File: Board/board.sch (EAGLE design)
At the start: 51 parts, among them IC1 L297, IC2 MEGA32-P, IC3 L298, J1 +12V, Q1 BC639, Q3 BC639, U2 DS1621+, X1 WATER_PUMP, X2 FAN, X5 SM_CD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

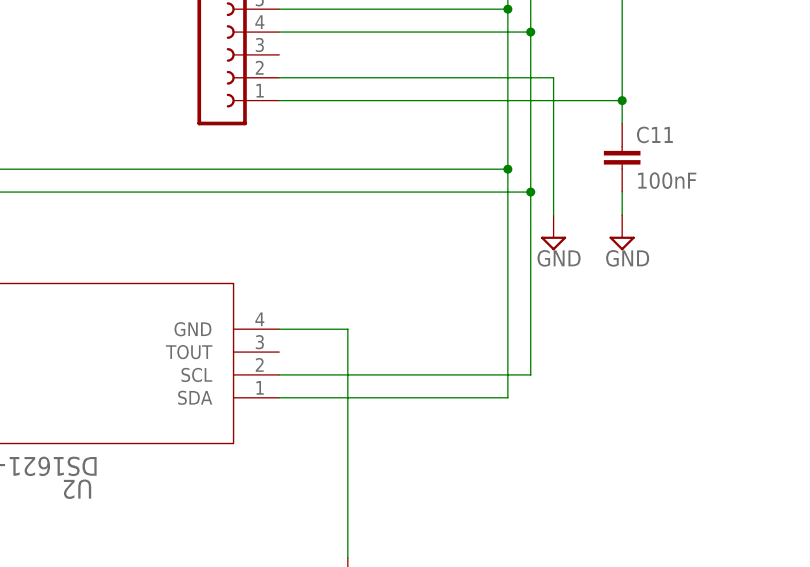
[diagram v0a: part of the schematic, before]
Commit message: SCL/SDA thermometer
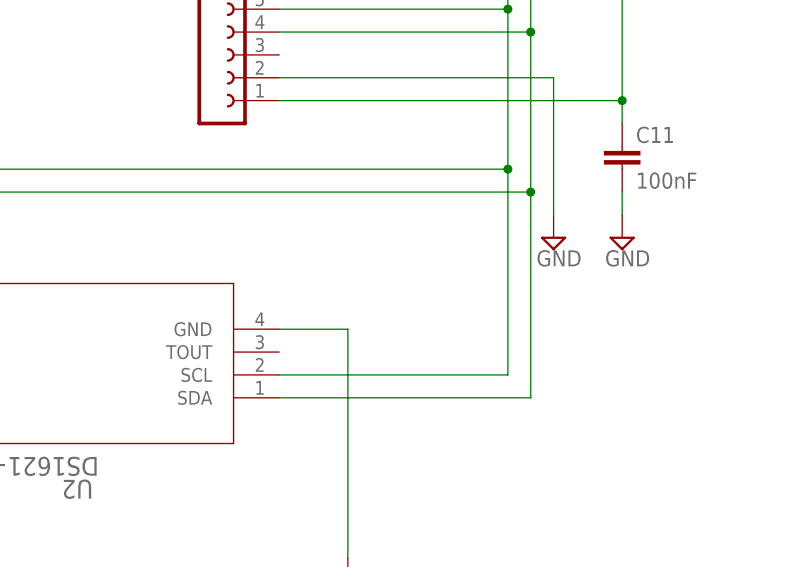
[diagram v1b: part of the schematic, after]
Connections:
- net N$35: now also U2.SDA; no longer U2.SCL
- net N$36: now also U2.SCL; no longer U2.SDA
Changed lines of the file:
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@@
 <grid distance="0.1" unitdist="inch" unit="inch" style="lines" multiple="1" display="no" altdistance="0.01" altunitdist="inch" altunit="inch"/>
 <layers>
-<layer number="1" name="Top" color="4" fill="1" visible="no" active="no"/>
-<layer number="2" name="Route2" color="1" fill="3" visible="no" active="no"/>
-<layer number="3" name="Route3" color="4" fill="3" visible="no" active="no"/>
-<layer number="4" name="Route4" color="1" fill="4" visible="no" active="no"/>
-<layer number="5" name="Route5" color="4" fill="4" visible="no" active="no"/>
-<layer number="6" name="Route6" color="1" fill="8" visible="no" active="no"/>
-<layer number="7" name="Route7" color="4" fill="8" visible="no" active="no"/>
-<layer number="8" name="Route8" color="1" fill="2" visible="no" active="no"/>
-<layer number="9" name="Route9" color="4" fill="2" visible="no" active="no"/>
-<layer number="10" name="Route10" color="1" fill="7" visible="no" active="no"/>
-<layer number="11" name="Route11" color="4" fill="7" visible="no" active="no"/>
-<layer number="12" name="Route12" color="1" fill="5" visible="no" active="no"/>
-<layer number="13" name="Route13" color="4" fill="5" visible="no" active="no"/>
-<layer number="14" name="Route14" color="1" fill="6" visible="no" active="no"/>
-<layer number="15" name="Route15" color="4" fill="6" visible="no" active="no"/>
-<layer number="16" name="Bottom" color="1" fill="1" visible="no" active="no"/>
-<layer number="17" name="Pads" color="2" fill="1" visible="no" active="no"/>
-<layer number="18" name="Vias" color="2" fill="1" visible="no" active="no"/>
-<layer number="19" name="Unrouted" color="6" fill="1" visible="no" active="no"/>
-<layer number="20" name="Dimension" color="24" fill="1" visible="no" active="no"/>
-<layer number="21" name="tPlace" color="7" fill="1" visible="no" active="no"/>
-<layer number="22" name="bPlace" color="7" fill="1" visible="no" active="no"/>
-<layer number="23" name="tOrigins" color="15" fill="1" visible="no" active="no"/>
-<layer number="24" name="bOrigins" color="15" fill="1" visible="no" active="no"/>
-<layer number="25" name="tNames" color="7" fill="1" visible="no" active="no"/>
-<layer number="26" name="bNames" color="7" fill="1" visible="no" active="no"/>
-<layer number="27" name="tValues" color="7" fill="1" visible="no" active="no"/>
-<layer number="28" name="bValues" color="7" fill="1" visible="no" active="no"/>
+<layer number="1" name="Top" color="4" fill="1" visible="yes" active="no"/>
+<layer number="2" name="Route2" color="1" fill="3" visible="yes" active="no"/>
+<layer number="3" name="Route3" color="4" fill="3" visible="yes" active="no"/>
+<layer number="4" name="Route4" color="1" fill="4" visible="yes" active="no"/>
+<layer number="5" name="Route5" color="4" fill="4" visible="yes" active="no"/>
+<layer number="6" name="Route6" color="1" fill="8" visible="yes" active="no"/>
+<layer number="7" name="Route7" color="4" fill="8" visible="yes" active="no"/>
+<layer number="8" name="Route8" color="1" fill="2" visible="yes" active="no"/>
+<layer number="9" name="Route9" color="4" fill="2" visible="yes" active="no"/>
+<layer number="10" name="Route10" color="1" fill="7" visible="yes" active="no"/>
+<layer number="11" name="Route11" color="4" fill="7" visible="yes" active="no"/>
+<layer number="12" name="Route12" color="1" fill="5" visible="yes" active="no"/>
+<layer number="13" name="Route13" color="4" fill="5" visible="yes" active="no"/>
+<layer number="14" name="Route14" color="1" fill="6" visible="yes" active="no"/>
+<layer number="15" name="Route15" color="4" fill="6" visible="yes" active="no"/>
+<layer number="16" name="Bottom" color="1" fill="1" visible="yes" active="no"/>
+<layer number="17" name="Pads" color="2" fill="1" visible="yes" active="no"/>
+<layer number="18" name="Vias" color="2" fill="1" visible="yes" active="no"/>
+<layer number="19" name="Unrouted" color="6" fill="1" visible="yes" active="no"/>
+<layer number="20" name="Dimension" color="24" fill="1" visible="yes" active="no"/>
+<layer number="21" name="tPlace" color="7" fill="1" visible="yes" active="no"/>
+<layer number="22" name="bPlace" color="7" fill="1" visible="yes" active="no"/>
+<layer number="23" name="tOrigins" color="15" fill="1" visible="yes" active="no"/>
+<layer number="24" name="bOrigins" color="15" fill="1" visible="yes" active="no"/>
+<layer number="25" name="tNames" color="7" fill="1" visible="yes" active="no"/>
+<layer number="26" name="bNames" color="7" fill="1" visible="yes" active="no"/>
+<layer number="27" name="tValues" color="7" fill="1" visible="yes" active="no"/>
+<layer number="28" name="bValues" color="7" fill="1" visible="yes" active="no"/>
 <layer number="29" name="tStop" color="7" fill="3" visible="no" active="no"/>
 <layer number="30" name="bStop" color="7" fill="6" visible="no" active="no"/>
@@
 <layer number="35" name="tGlue" color="7" fill="4" visible="no" active="no"/>
 <layer number="36" name="bGlue" color="7" fill="5" visible="no" active="no"/>
-<layer number="37" name="tTest" color="7" fill="1" visible="no" active="no"/>
-<layer number="38" name="bTest" color="7" fill="1" visible="no" active="no"/>
+<layer number="37" name="tTest" color="7" fill="1" visible="yes" active="no"/>
+<layer number="38" name="bTest" color="7" fill="1" visible="yes" active="no"/>
 <layer number="39" name="tKeepout" color="4" fill="11" visible="no" active="no"/>
 <layer number="40" name="bKeepout" color="1" fill="11" visible="no" active="no"/>
@@
 <layer number="44" name="Drills" color="7" fill="1" visible="no" active="no"/>
 <layer number="45" name="Holes" color="7" fill="1" visible="no" active="no"/>
-<layer number="46" name="Milling" color="3" fill="1" visible="no" active="no"/>
-<layer number="47" name="Measures" color="7" fill="1" visible="no" active="no"/>
-<layer number="48" name="Document" color="7" fill="1" visible="no" active="no"/>
-<layer number="49" name="Reference" color="7" fill="1" visible="no" active="no"/>
-<layer number="50" name="dxf" color="7" fill="1" visible="no" active="no"/>
-<layer number="51" name="tDocu" color="7" fill="1" visible="no" active="no"/>
-<layer number="52" name="bDocu" color="7" fill="1" visible="no" active="no"/>
+<layer number="46" name="Milling" color="3" fill="1" visible="yes" active="no"/>
+<layer number="47" name="Measures" color="7" fill="1" visible="yes" active="no"/>
+<layer number="48" name="Document" color="7" fill="1" visible="yes" active="no"/>
+<layer number="49" name="Reference" color="7" fill="1" visible="yes" active="no"/>
+<layer number="50" name="dxf" color="7" fill="1" visible="yes" active="no"/>
+<layer number="51" name="tDocu" color="7" fill="1" visible="yes" active="no"/>
+<layer number="52" name="bDocu" color="7" fill="1" visible="yes" active="no"/>
 <layer number="88" name="SimResults" color="9" fill="1" visible="yes" active="yes"/>
 <layer number="89" name="SimProbes" color="9" fill="1" visible="yes" active="yes"/>
@@
 <wire x1="-83.82" y1="-86.36" x2="-83.82" y2="-104.14" width="0.1524" layer="91"/>
 <junction x="-83.82" y="-86.36"/>
-<pinref part="U2" gate="A" pin="SCL"/>
-<wire x1="-83.82" y1="-104.14" x2="-83.82" y2="-124.46" width="0.1524" layer="91"/>
-<wire x1="-83.82" y1="-124.46" x2="-111.76" y2="-124.46" width="0.1524" layer="91"/>
+<wire x1="-83.82" y1="-104.14" x2="-83.82" y2="-127" width="0.1524" layer="91"/>
 <pinref part="R8" gate="G$1" pin="1"/>
 <wire x1="-83.82" y1="-104.14" x2="-149.86" y2="-104.14" width="0.1524" layer="91"/>
 <wire x1="-149.86" y1="-104.14" x2="-149.86" y2="-83.82" width="0.1524" layer="91"/>
 <junction x="-83.82" y="-104.14"/>
+<pinref part="U2" gate="A" pin="SDA"/>
+<wire x1="-83.82" y1="-127" x2="-111.76" y2="-127" width="0.1524" layer="91"/>
 </segment>
 </net>
@@
 <wire x1="-86.36" y1="-83.82" x2="-86.36" y2="-101.6" width="0.1524" layer="91"/>
 <junction x="-86.36" y="-83.82"/>
-<pinref part="U2" gate="A" pin="SDA"/>
-<wire x1="-86.36" y1="-101.6" x2="-86.36" y2="-127" width="0.1524" layer="91"/>
-<wire x1="-86.36" y1="-127" x2="-111.76" y2="-127" width="0.1524" layer="91"/>
 <pinref part="R6" gate="G$1" pin="1"/>
 <wire x1="-86.36" y1="-101.6" x2="-160.02" y2="-101.6" width="0.1524" layer="91"/>
 <wire x1="-160.02" y1="-101.6" x2="-160.02" y2="-83.82" width="0.1524" layer="91"/>
+<pinref part="U2" gate="A" pin="SCL"/>
+<wire x1="-111.76" y1="-124.46" x2="-86.36" y2="-124.46" width="0.1524" layer="91"/>
+<wire x1="-86.36" y1="-124.46" x2="-86.36" y2="-101.6" width="0.1524" layer="91"/>
 <junction x="-86.36" y="-101.6"/>
 </segment>

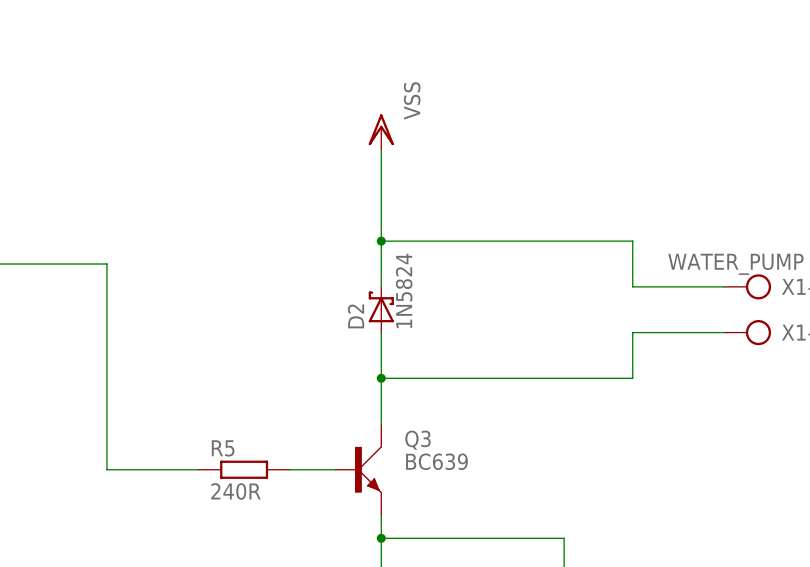
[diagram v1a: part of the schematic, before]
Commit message: Rename 1N5824 - 1N5822
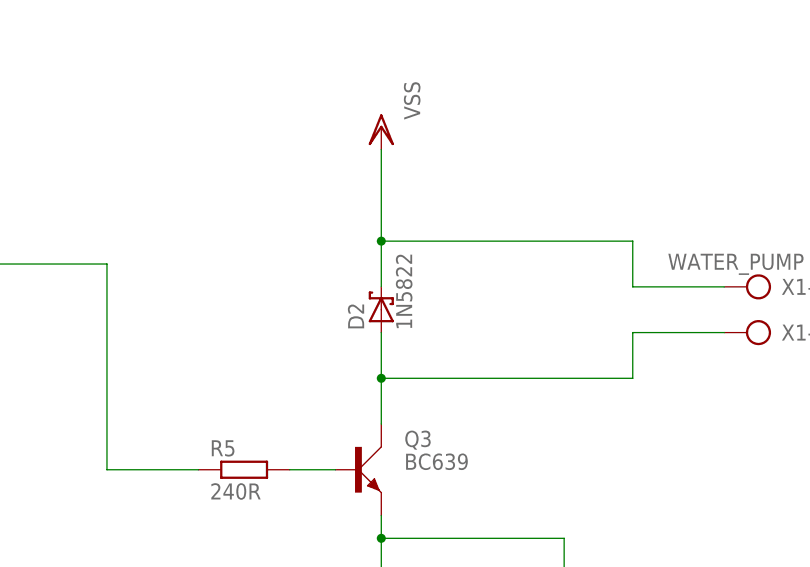
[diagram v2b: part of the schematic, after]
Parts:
- D2: value 1N5824 -> 1N5822
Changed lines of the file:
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@@
 <grid distance="0.1" unitdist="inch" unit="inch" style="lines" multiple="1" display="no" altdistance="0.01" altunitdist="inch" altunit="inch"/>
 <layers>
-<layer number="1" name="Top" color="4" fill="1" visible="yes" active="no"/>
-<layer number="2" name="Route2" color="1" fill="3" visible="yes" active="no"/>
-<layer number="3" name="Route3" color="4" fill="3" visible="yes" active="no"/>
-<layer number="4" name="Route4" color="1" fill="4" visible="yes" active="no"/>
-<layer number="5" name="Route5" color="4" fill="4" visible="yes" active="no"/>
-<layer number="6" name="Route6" color="1" fill="8" visible="yes" active="no"/>
-<layer number="7" name="Route7" color="4" fill="8" visible="yes" active="no"/>
-<layer number="8" name="Route8" color="1" fill="2" visible="yes" active="no"/>
-<layer number="9" name="Route9" color="4" fill="2" visible="yes" active="no"/>
-<layer number="10" name="Route10" color="1" fill="7" visible="yes" active="no"/>
-<layer number="11" name="Route11" color="4" fill="7" visible="yes" active="no"/>
-<layer number="12" name="Route12" color="1" fill="5" visible="yes" active="no"/>
-<layer number="13" name="Route13" color="4" fill="5" visible="yes" active="no"/>
-<layer number="14" name="Route14" color="1" fill="6" visible="yes" active="no"/>
-<layer number="15" name="Route15" color="4" fill="6" visible="yes" active="no"/>
-<layer number="16" name="Bottom" color="1" fill="1" visible="yes" active="no"/>
-<layer number="17" name="Pads" color="2" fill="1" visible="yes" active="no"/>
-<layer number="18" name="Vias" color="2" fill="1" visible="yes" active="no"/>
-<layer number="19" name="Unrouted" color="6" fill="1" visible="yes" active="no"/>
-<layer number="20" name="Dimension" color="24" fill="1" visible="yes" active="no"/>
-<layer number="21" name="tPlace" color="7" fill="1" visible="yes" active="no"/>
-<layer number="22" name="bPlace" color="7" fill="1" visible="yes" active="no"/>
-<layer number="23" name="tOrigins" color="15" fill="1" visible="yes" active="no"/>
-<layer number="24" name="bOrigins" color="15" fill="1" visible="yes" active="no"/>
-<layer number="25" name="tNames" color="7" fill="1" visible="yes" active="no"/>
-<layer number="26" name="bNames" color="7" fill="1" visible="yes" active="no"/>
-<layer number="27" name="tValues" color="7" fill="1" visible="yes" active="no"/>
-<layer number="28" name="bValues" color="7" fill="1" visible="yes" active="no"/>
+<layer number="1" name="Top" color="4" fill="1" visible="no" active="no"/>
+<layer number="2" name="Route2" color="1" fill="3" visible="no" active="no"/>
+<layer number="3" name="Route3" color="4" fill="3" visible="no" active="no"/>
+<layer number="4" name="Route4" color="1" fill="4" visible="no" active="no"/>
+<layer number="5" name="Route5" color="4" fill="4" visible="no" active="no"/>
+<layer number="6" name="Route6" color="1" fill="8" visible="no" active="no"/>
+<layer number="7" name="Route7" color="4" fill="8" visible="no" active="no"/>
+<layer number="8" name="Route8" color="1" fill="2" visible="no" active="no"/>
+<layer number="9" name="Route9" color="4" fill="2" visible="no" active="no"/>
+<layer number="10" name="Route10" color="1" fill="7" visible="no" active="no"/>
+<layer number="11" name="Route11" color="4" fill="7" visible="no" active="no"/>
+<layer number="12" name="Route12" color="1" fill="5" visible="no" active="no"/>
+<layer number="13" name="Route13" color="4" fill="5" visible="no" active="no"/>
+<layer number="14" name="Route14" color="1" fill="6" visible="no" active="no"/>
+<layer number="15" name="Route15" color="4" fill="6" visible="no" active="no"/>
+<layer number="16" name="Bottom" color="1" fill="1" visible="no" active="no"/>
+<layer number="17" name="Pads" color="2" fill="1" visible="no" active="no"/>
+<layer number="18" name="Vias" color="2" fill="1" visible="no" active="no"/>
+<layer number="19" name="Unrouted" color="6" fill="1" visible="no" active="no"/>
+<layer number="20" name="Dimension" color="24" fill="1" visible="no" active="no"/>
+<layer number="21" name="tPlace" color="7" fill="1" visible="no" active="no"/>
+<layer number="22" name="bPlace" color="7" fill="1" visible="no" active="no"/>
+<layer number="23" name="tOrigins" color="15" fill="1" visible="no" active="no"/>
+<layer number="24" name="bOrigins" color="15" fill="1" visible="no" active="no"/>
+<layer number="25" name="tNames" color="7" fill="1" visible="no" active="no"/>
+<layer number="26" name="bNames" color="7" fill="1" visible="no" active="no"/>
+<layer number="27" name="tValues" color="7" fill="1" visible="no" active="no"/>
+<layer number="28" name="bValues" color="7" fill="1" visible="no" active="no"/>
 <layer number="29" name="tStop" color="7" fill="3" visible="no" active="no"/>
 <layer number="30" name="bStop" color="7" fill="6" visible="no" active="no"/>
@@
 <layer number="35" name="tGlue" color="7" fill="4" visible="no" active="no"/>
 <layer number="36" name="bGlue" color="7" fill="5" visible="no" active="no"/>
-<layer number="37" name="tTest" color="7" fill="1" visible="yes" active="no"/>
-<layer number="38" name="bTest" color="7" fill="1" visible="yes" active="no"/>
+<layer number="37" name="tTest" color="7" fill="1" visible="no" active="no"/>
+<layer number="38" name="bTest" color="7" fill="1" visible="no" active="no"/>
 <layer number="39" name="tKeepout" color="4" fill="11" visible="no" active="no"/>
 <layer number="40" name="bKeepout" color="1" fill="11" visible="no" active="no"/>
@@
 <layer number="44" name="Drills" color="7" fill="1" visible="no" active="no"/>
 <layer number="45" name="Holes" color="7" fill="1" visible="no" active="no"/>
-<layer number="46" name="Milling" color="3" fill="1" visible="yes" active="no"/>
-<layer number="47" name="Measures" color="7" fill="1" visible="yes" active="no"/>
-<layer number="48" name="Document" color="7" fill="1" visible="yes" active="no"/>
-<layer number="49" name="Reference" color="7" fill="1" visible="yes" active="no"/>
-<layer number="50" name="dxf" color="7" fill="1" visible="yes" active="no"/>
-<layer number="51" name="tDocu" color="7" fill="1" visible="yes" active="no"/>
-<layer number="52" name="bDocu" color="7" fill="1" visible="yes" active="no"/>
+<layer number="46" name="Milling" color="3" fill="1" visible="no" active="no"/>
+<layer number="47" name="Measures" color="7" fill="1" visible="no" active="no"/>
+<layer number="48" name="Document" color="7" fill="1" visible="no" active="no"/>
+<layer number="49" name="Reference" color="7" fill="1" visible="no" active="no"/>
+<layer number="50" name="dxf" color="7" fill="1" visible="no" active="no"/>
+<layer number="51" name="tDocu" color="7" fill="1" visible="no" active="no"/>
+<layer number="52" name="bDocu" color="7" fill="1" visible="no" active="no"/>
 <layer number="88" name="SimResults" color="9" fill="1" visible="yes" active="yes"/>
 <layer number="89" name="SimProbes" color="9" fill="1" visible="yes" active="yes"/>
@@
 <part name="R4" library="rcl" deviceset="R-EU_" device="0207/12" value="470R"/>
 <part name="SUPPLY19" library="supply2" deviceset="GND" device=""/>
-<part name="D2" library="diode" deviceset="1N581*" device="" technology="9-B" value="1N5824"/>
+<part name="D2" library="diode" deviceset="1N581*" device="" technology="9-B" value="1N5822"/>
 <part name="SUPPLY20" library="supply2" deviceset="GND" device=""/>
 <part name="R5" library="rcl" deviceset="R-EU_" device="0207/12" value="240R"/>
